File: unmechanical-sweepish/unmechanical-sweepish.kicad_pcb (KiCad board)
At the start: 4 copper layers, 214 x 145.5 mm, 168 parts, among them J1 HytePro M, J2 USB_C_Receptacle_USB2.0, J3 M, J4 HytePro F, J5 USB_C_Receptacle_USB2.0, J6 M, Q1 AO3400A, Q2 AO3400A, SW1 B/R, SW2 B/R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

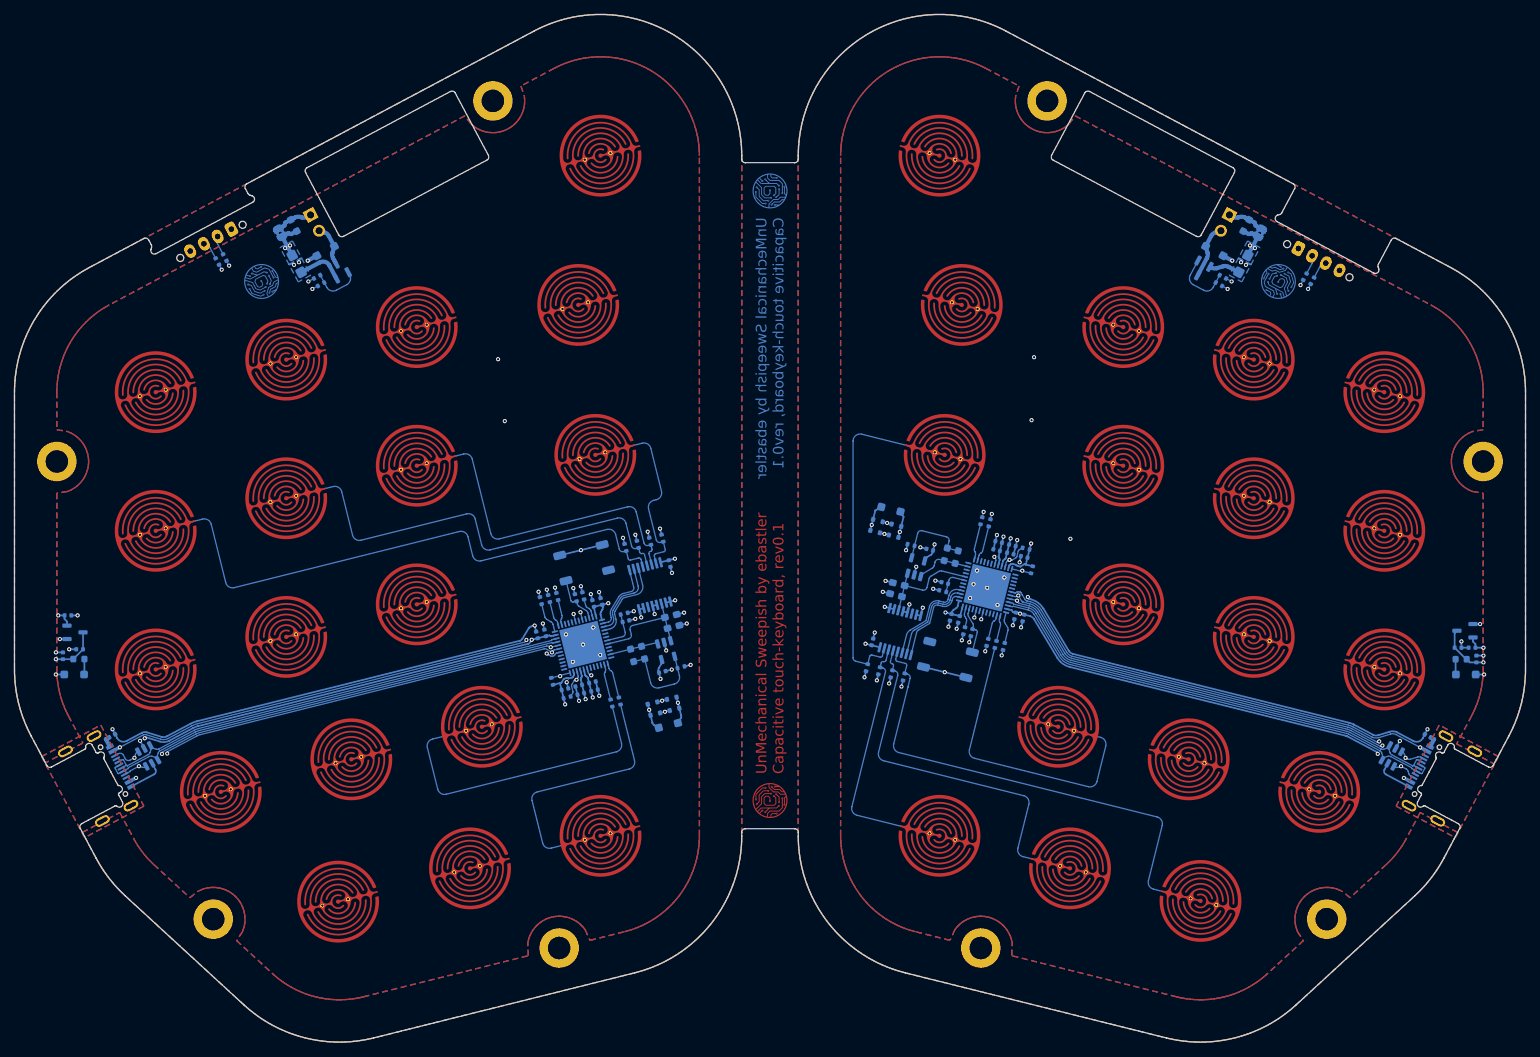
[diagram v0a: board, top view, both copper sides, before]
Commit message: Migrate to v8
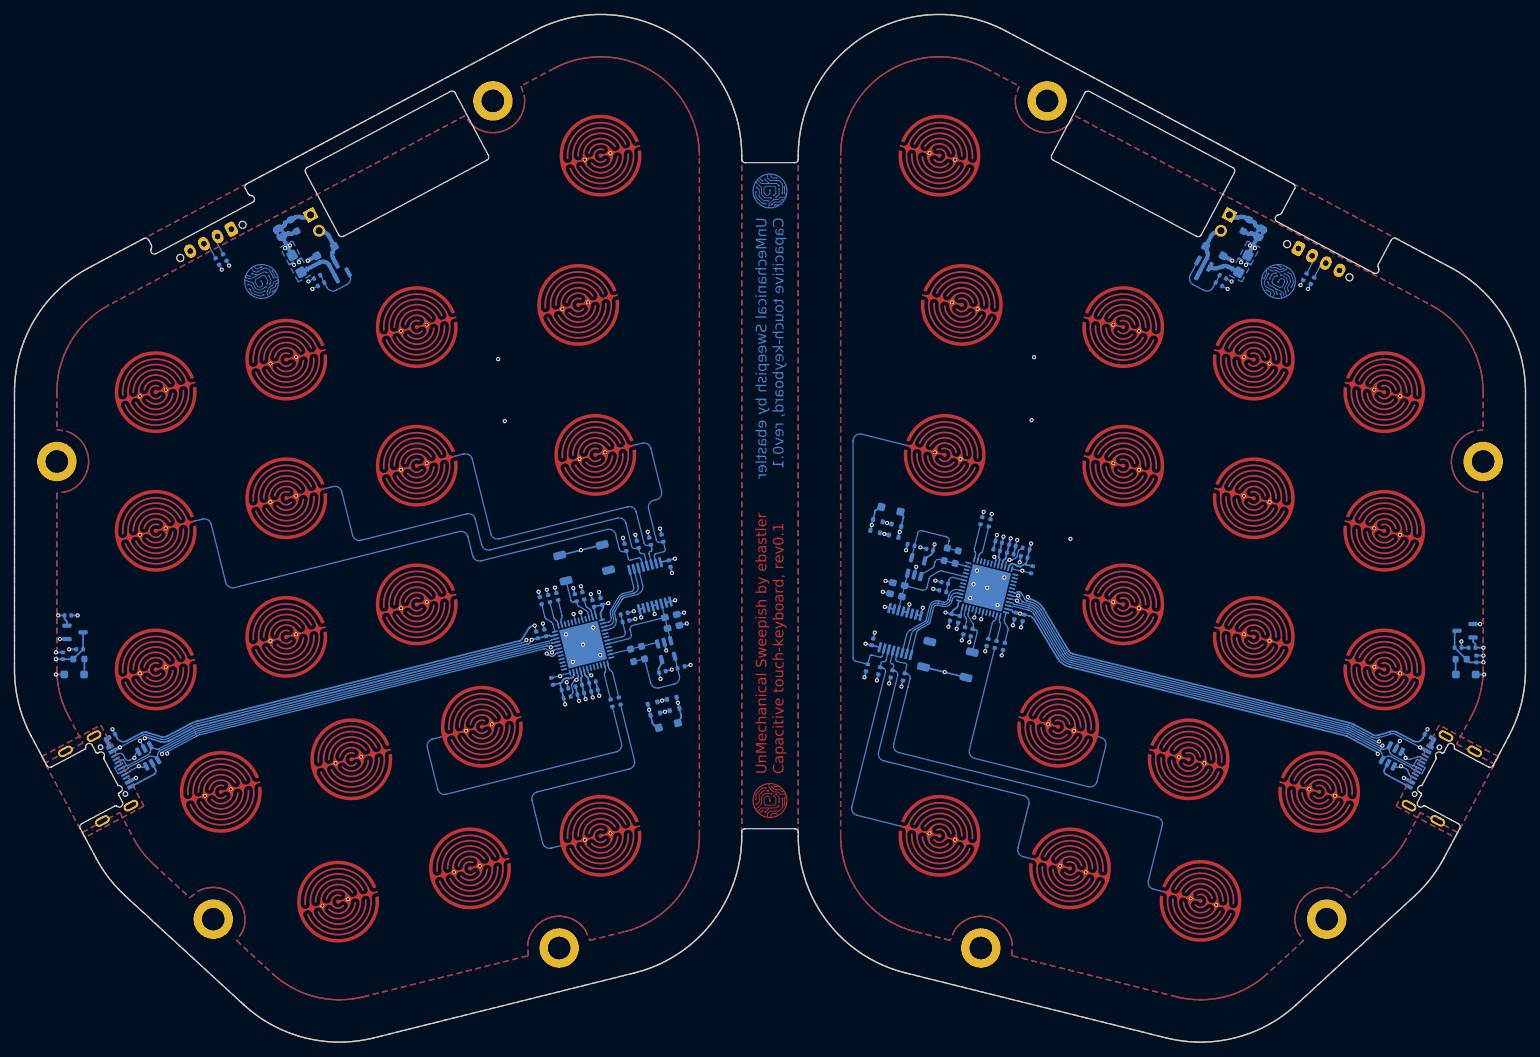
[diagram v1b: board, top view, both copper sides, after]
